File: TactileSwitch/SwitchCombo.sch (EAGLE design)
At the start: 4 parts, among them J1 CONN_3, J2 CONN_3

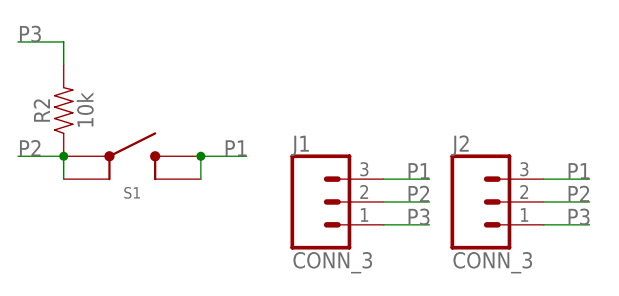
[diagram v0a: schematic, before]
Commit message: Updated tactile switch combo resistor
Changed the resistor layout on the combo switch breakout to be more relaxed and work more easily with standard 1/4 W resistors
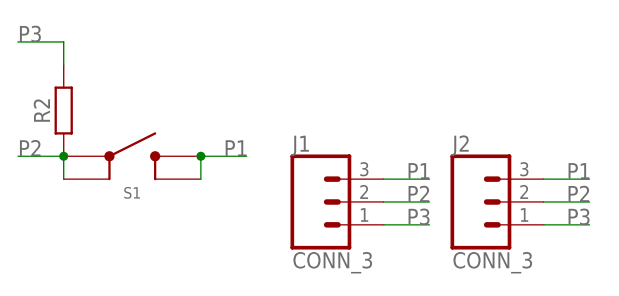
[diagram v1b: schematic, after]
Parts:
- R2: device SparkFun-Resistors:10KOHM-HORIZ-1/4W-1% -> bschulz_passives:R-EU_TH_0.4"
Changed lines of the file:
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@@
 <?xml version="1.0" encoding="utf-8"?>
 <!DOCTYPE eagle SYSTEM "eagle.dtd">
-<eagle version="9.4.2">
+<eagle version="9.6.2">
 <drawing>
 <settings>
@@
 <layer number="115" name="ReferenceISLANDS" color="7" fill="1" visible="no" active="yes"/>
 <layer number="116" name="Patch_BOT" color="7" fill="1" visible="no" active="yes"/>
+<layer number="117" name="PM_Ref" color="7" fill="1" visible="no" active="no"/>
 <layer number="118" name="Rect_Pads" color="7" fill="1" visible="no" active="yes"/>
+<layer number="119" name="PF_Ref" color="7" fill="1" visible="no" active="no"/>
+<layer number="120" name="WFL_Ref" color="7" fill="1" visible="no" active="no"/>
 <layer number="121" name="_tsilk" color="7" fill="1" visible="no" active="yes"/>
 <layer number="122" name="_bsilk" color="7" fill="1" visible="no" active="yes"/>
@@
 <part name="J1" library="bschulz" deviceset="CONN_3" device=""/>
 <part name="J2" library="bschulz" deviceset="CONN_3" device=""/>
-<part name="R2" library="SparkFun-Resistors" library_urn="urn:adsk.eagle:library:532" deviceset="10KOHM" device="-HORIZ-1/4W-1%" package3d_urn="urn:adsk.eagle:package:39658/1" value="10k"/>
+<part name="R2" library="bschulz_passives" deviceset="R-EU_" device="TH_0.4&quot;" value="10k"/>
 </parts>
 <sheets>
@@
 <instance part="R2" gate="G$1" x="5.08" y="30.48" smashed="yes" rot="R90">
 <attribute name="NAME" x="3.556" y="30.48" size="1.778" layer="95" font="vector" rot="R90" align="bottom-center"/>
-<attribute name="VALUE" x="6.604" y="30.48" size="1.778" layer="96" font="vector" rot="R90" align="top-center"/>
 </instance>
 </instances>
@@
 </drawing>
 <compatibility>
-<note version="8.2" severity="warning">
-Since Version 8.2, EAGLE supports online libraries. The ids
-of those online libraries will not be understood (or retained)
-with this version.
-</note>
 <note version="8.3" severity="warning">
 Since Version 8.3, EAGLE supports URNs for individual library
@@
 will not be understood (or retained) with this version.
 </note>
-<note version="8.3" severity="warning">
-Since Version 8.3, EAGLE supports the association of 3D packages
-with devices in libraries, schematics, and board files. Those 3D
-packages will not be understood (or retained) with this version.
-</note>
 </compatibility>
